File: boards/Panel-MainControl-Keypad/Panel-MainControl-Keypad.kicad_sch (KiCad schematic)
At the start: 22 parts, among them J1 Conn_01x10, J2 Conn_01x10, SW1 SW_Push, SW10 SW_Push, SW11 RotaryEncoder_Switch, SW12 RotaryEncoder_Switch, SW2 SW_Push, SW3 SW_Push, SW4 SW_Push, SW5 SW_Push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

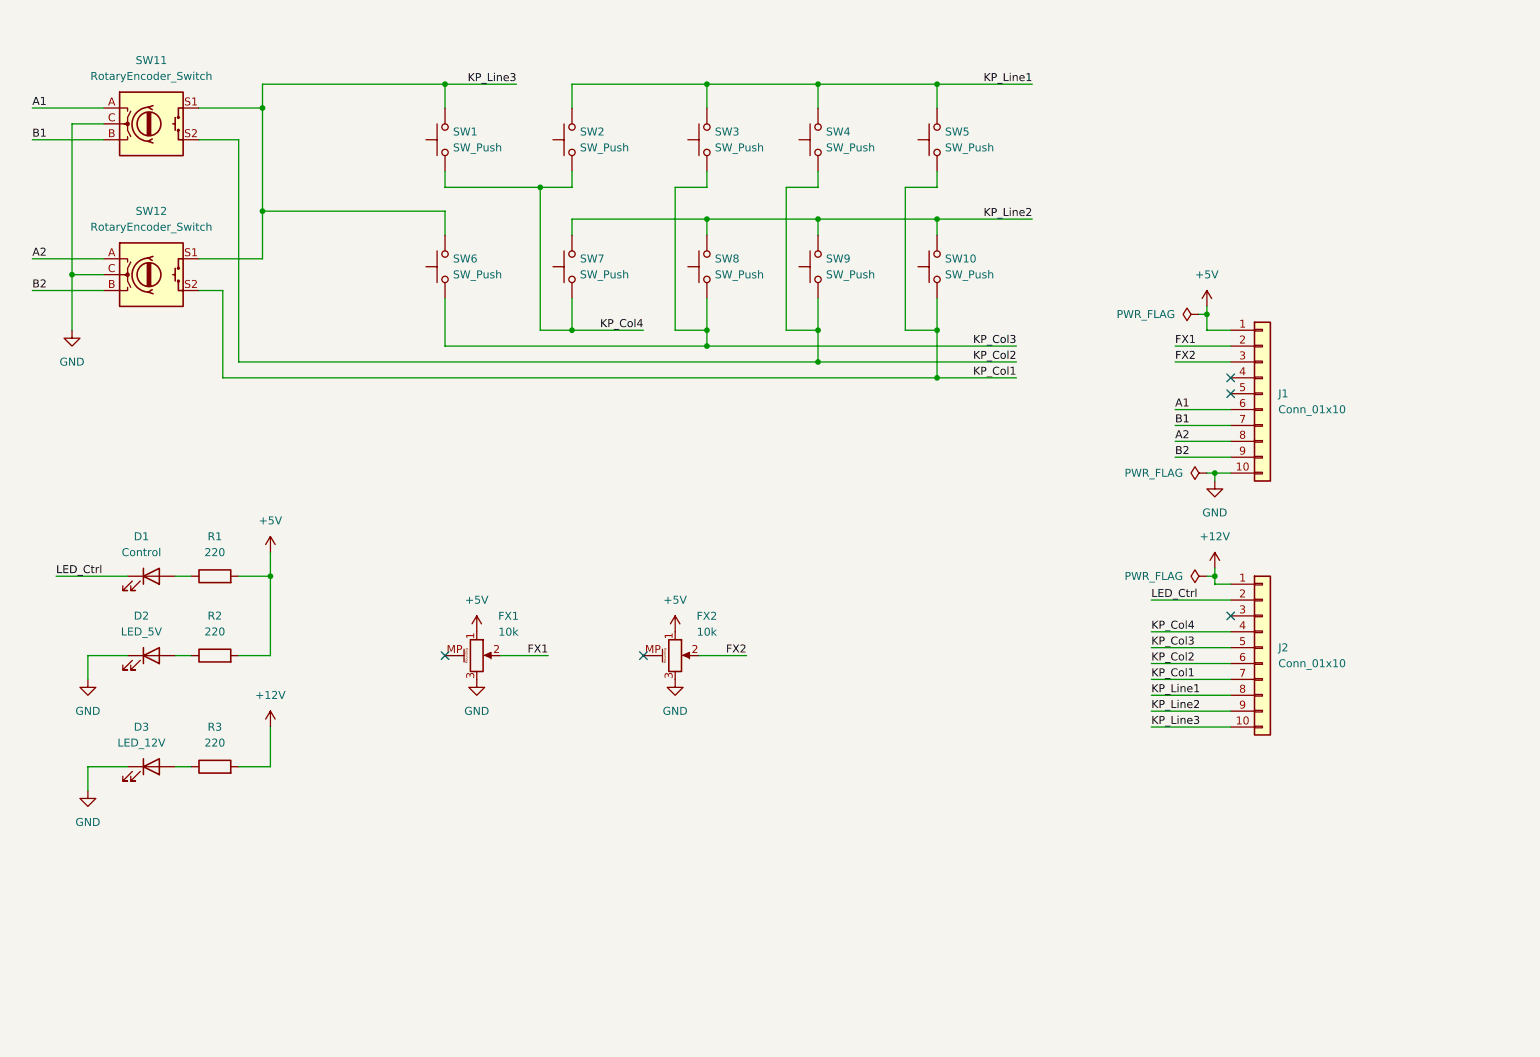
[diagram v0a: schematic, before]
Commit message: Finished PCB layouts for panel keypad
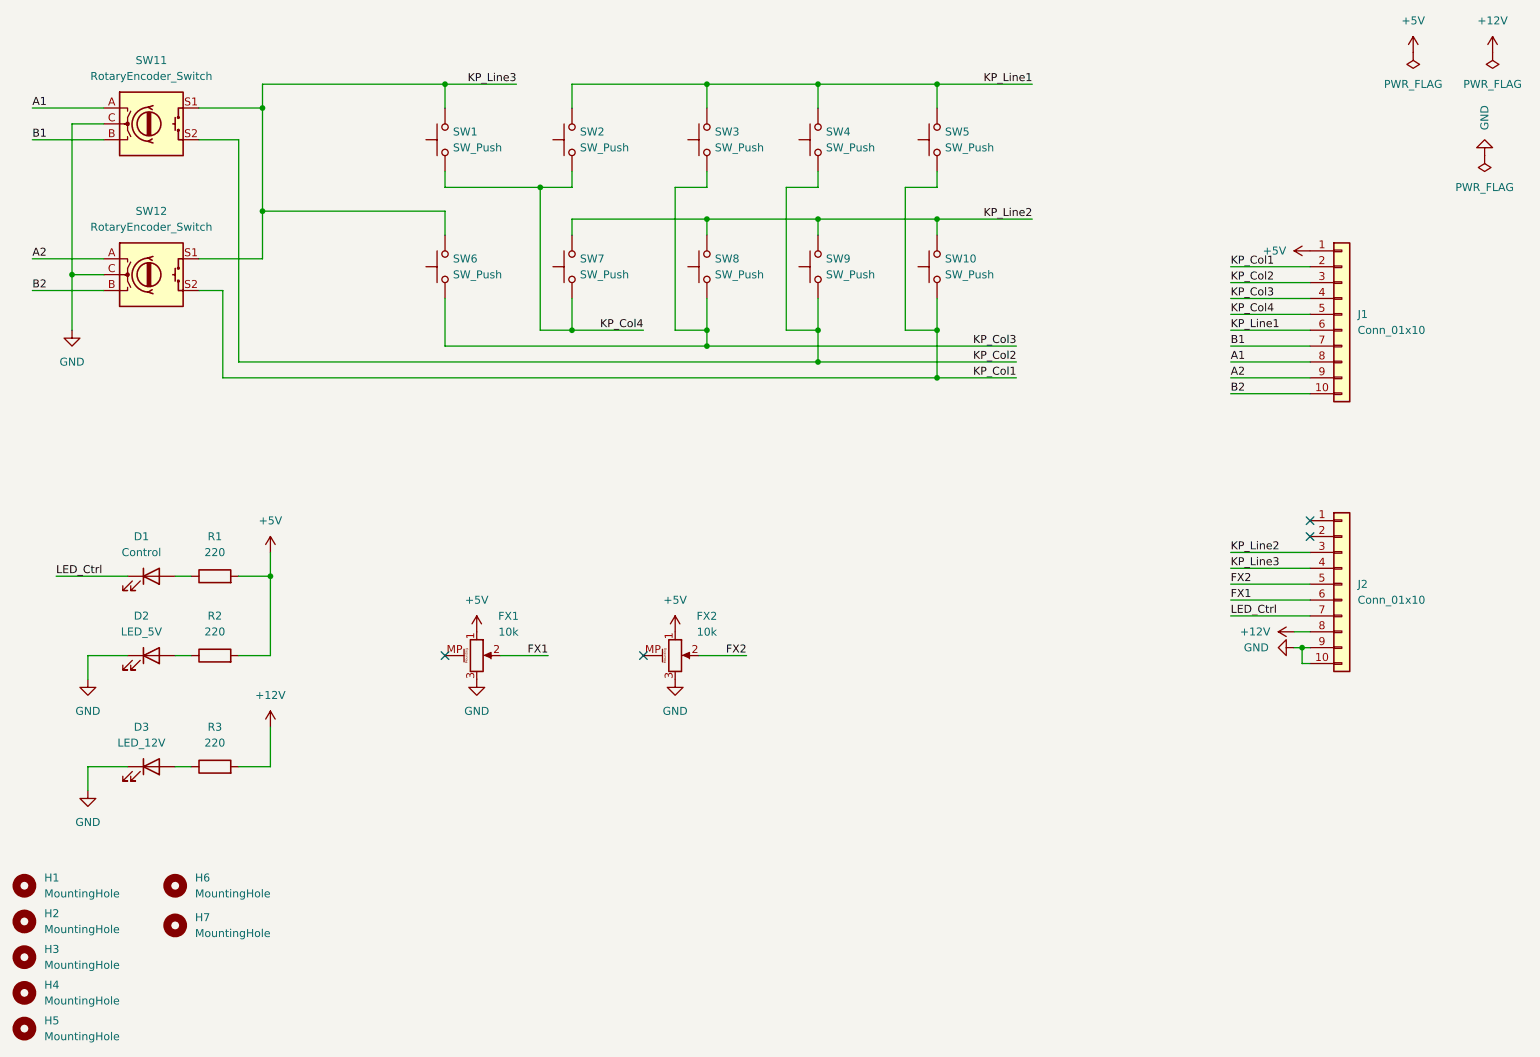
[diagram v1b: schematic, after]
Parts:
- added H1, H2, H3, H4, H5, H6, H7: MountingHole, MountingHole:MountingHole_2.7mm_M2.5, symbol Mechanical:MountingHole
- D1, D2, D3: footprint (none) -> LED_THT:LED_Rectangular_W5.0mm_H2.0mm
- J1, J2: footprint (none) -> Connector_PinHeader_2.00mm:PinHeader_1x10_P2.00mm_Vertical
- SW1, SW10, SW2, SW3, SW4, SW5, SW6, SW7, SW8, SW9: footprint Button_Switch_SMD:SW_MEC_5GSH9 -> Button_Switch_THT:SW_PUSH_6mm_H9.5mm
- SW11, SW12: footprint (none) -> SnapEDA:RotaryEncoder_Switch-PEC11R-4215F
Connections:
- net +12V: now also J2.8 (Pin_8); no longer J2.1 (Pin_1)
- net A1: now also J1.8 (Pin_8); no longer J1.6 (Pin_6)
- net A2: now also J1.9 (Pin_9); no longer J1.8 (Pin_8)
- net B2: now also J1.10 (Pin_10); no longer J1.9 (Pin_9)
- net FX1: now also J2.6 (Pin_6); no longer J1.2 (Pin_2)
- net FX2: now also J2.5 (Pin_5); no longer J1.3 (Pin_3)
- net GND: now also J2.10 (Pin_10), J2.9 (Pin_9); no longer J1.10 (Pin_10)
- net KP_Col1: now also J1.2 (Pin_2); no longer J2.7 (Pin_7)
- net KP_Col2: now also J1.3 (Pin_3); no longer J2.6 (Pin_6)
- net KP_Col3: now also J1.4 (Pin_4); no longer J2.5 (Pin_5)
- net KP_Col4: now also J1.5 (Pin_5); no longer J2.4 (Pin_4)
- net KP_Line1: now also J1.6 (Pin_6); no longer J2.8 (Pin_8)
- net KP_Line2: now also J2.3 (Pin_3); no longer J2.9 (Pin_9)
- net KP_Line3: now also J2.4 (Pin_4); no longer J2.10 (Pin_10)
- net LED_Ctrl: now also J2.7 (Pin_7); no longer J2.2 (Pin_2)
- no-connect marks 5 -> 4

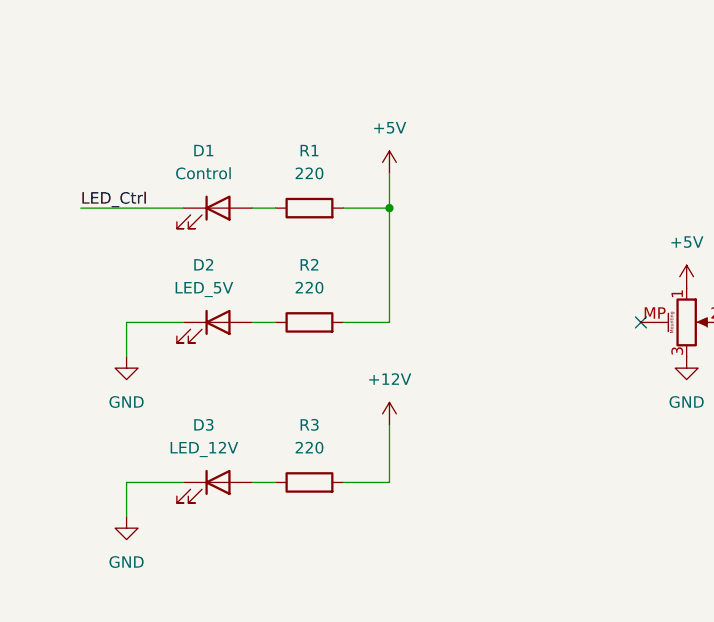
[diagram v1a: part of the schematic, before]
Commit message: Updated LED resistor values
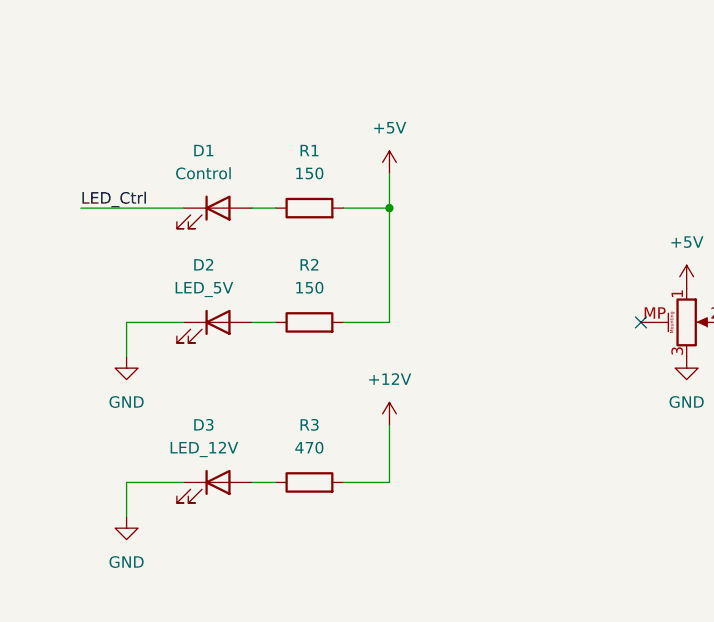
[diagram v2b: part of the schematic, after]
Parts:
- R1, R2: value 220 -> 150
- R3: value 220 -> 470
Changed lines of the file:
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@@
 			)
 		)
-		(property "Value" "220"
+		(property "Value" "150"
 			(at 59.69 110.49 90)
 			(effects
@@
 			)
 		)
-		(property "Value" "220"
+		(property "Value" "470"
 			(at 59.69 140.97 90)
 			(effects
@@
 			)
 		)
-		(property "Value" "220"
+		(property "Value" "150"
 			(at 59.69 123.19 90)
 			(effects

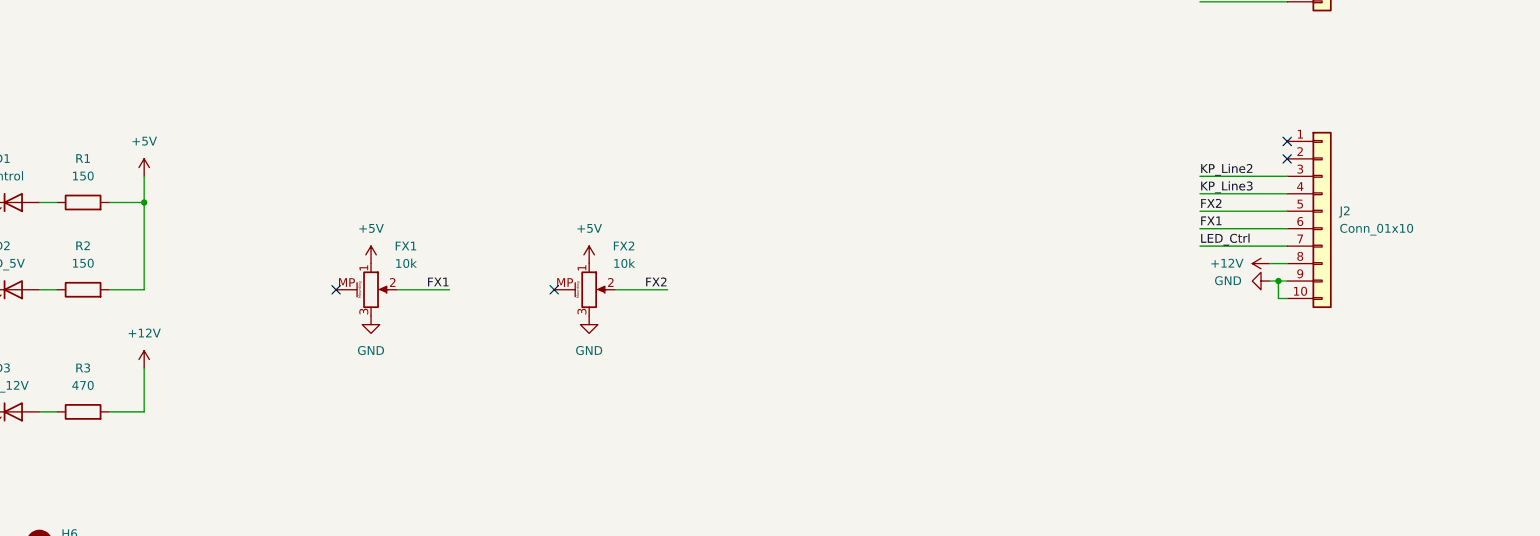
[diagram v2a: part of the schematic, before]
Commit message: Fixed using 5V from main power for PWR LED
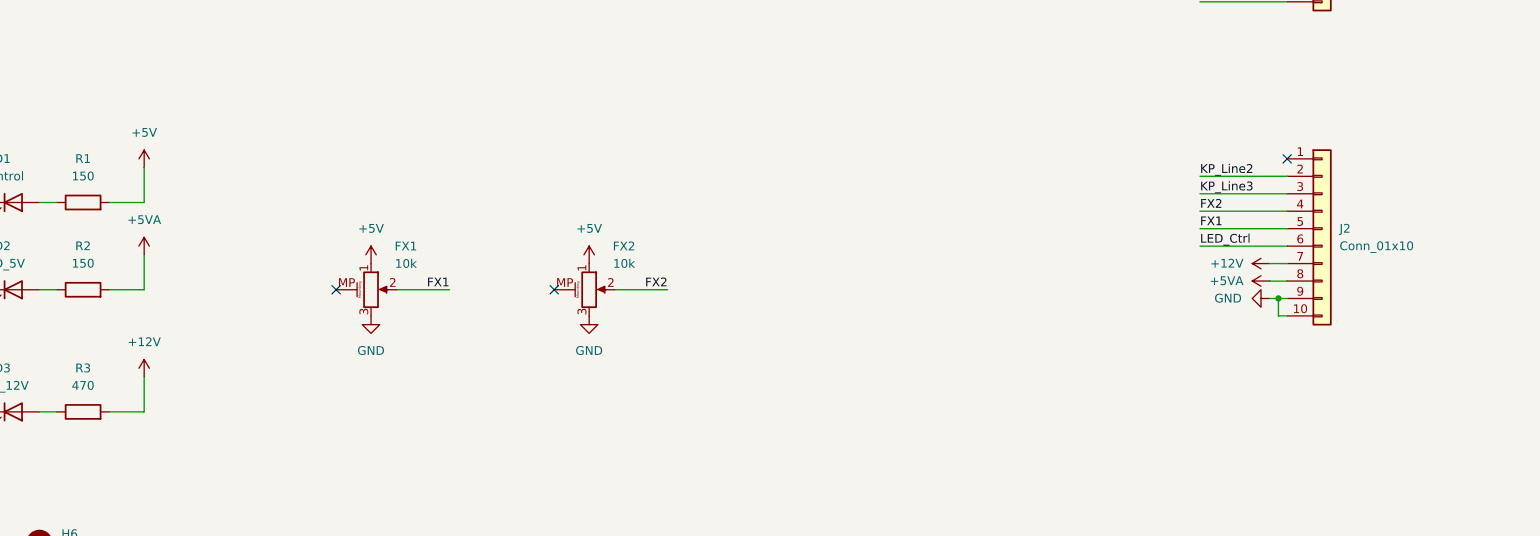
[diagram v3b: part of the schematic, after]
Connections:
- net +12V: now also J2.7 (Pin_7); no longer J2.8 (Pin_8)
- net +5V: no longer R2.2
- net FX1: now also J2.5 (Pin_5); no longer J2.6 (Pin_6)
- net FX2: now also J2.4 (Pin_4); no longer J2.5 (Pin_5)
- net KP_Line2: now also J2.2 (Pin_2); no longer J2.3 (Pin_3)
- net KP_Line3: now also J2.3 (Pin_3); no longer J2.4 (Pin_4)
- net LED_Ctrl: now also J2.6 (Pin_6); no longer J2.7 (Pin_7)
- new net +5VA: J2.8 (Pin_8), R2.2
- no-connect marks 4 -> 3
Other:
- moved on the sheet: J2
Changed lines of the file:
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@@
 	)
 	(junction
-		(at 233.68 125.73)
+		(at 233.68 128.27)
 		(diameter 0)
 		(color 0 0 0 0)
@@
 	)
 	(junction
-		(at 68.58 114.3)
-		(diameter 0)
-		(color 0 0 0 0)
-	)
-	(junction
 		(at 175.26 82.55)
 		(diameter 0)
@@
 	)
 	(no_connect
-		(at 234.95 105.41)
-	)
-	(no_connect
 		(at 234.95 107.95)
 	)
@@
 	(wire
 		(pts
+			(xy 232.41 125.73) (xy 234.95 125.73)
+		)
+		(stroke
+			(width 0)
+			(type default)
+		)
+	)
+	(wire
+		(pts
 			(xy 138.43 77.47) (xy 187.96 77.47)
 		)
@@
 	(wire
 		(pts
-			(xy 233.68 125.73) (xy 232.41 125.73)
+			(xy 233.68 128.27) (xy 232.41 128.27)
 		)
 		(stroke
@@
 	(wire
 		(pts
-			(xy 96.52 55.88) (xy 67.31 55.88)
+			(xy 68.58 121.92) (xy 68.58 127)
 		)
 		(stroke
@@
 	(wire
 		(pts
-			(xy 234.95 125.73) (xy 233.68 125.73)
+			(xy 96.52 55.88) (xy 67.31 55.88)
 		)
 		(stroke
@@
 	(wire
 		(pts
-			(xy 111.76 74.93) (xy 116.84 74.93)
+			(xy 234.95 128.27) (xy 233.68 128.27)
 		)
 		(stroke
@@
 	(wire
 		(pts
-			(xy 68.58 127) (xy 68.58 114.3)
+			(xy 111.76 74.93) (xy 116.84 74.93)
 		)
 		(stroke
@@
 	(wire
 		(pts
-			(xy 233.68 125.73) (xy 233.68 128.27)
+			(xy 233.68 128.27) (xy 233.68 130.81)
 		)
 		(stroke
@@
 	(wire
 		(pts
-			(xy 68.58 110.49) (xy 68.58 114.3)
+			(xy 68.58 109.22) (xy 68.58 114.3)
 		)
 		(stroke
@@
 	(wire
 		(pts
-			(xy 68.58 138.43) (xy 68.58 144.78)
+			(xy 68.58 139.7) (xy 68.58 144.78)
 		)
 		(stroke
@@
 	(wire
 		(pts
-			(xy 234.95 128.27) (xy 233.68 128.27)
+			(xy 234.95 130.81) (xy 233.68 130.81)
 		)
 		(stroke
@@
 	)
 	(symbol
+		(lib_id "power:+5VA")
+		(at 232.41 125.73 90)
+		(unit 1)
+		(exclude_from_sim no)
+		(in_bom yes)
+		(on_board yes)
+		(dnp no)
+		(fields_autoplaced yes)
+		(property "Reference" "#PWR016"
+			(at 236.22 125.73 0)
+			(effects
+				(font
+					(size 1.27 1.27)
+				)
+				(hide yes)
+			)
+		)
+		(property "Value" "+5VA"
+			(at 228.6 125.7299 90)
+			(effects
+				(font
+					(size 1.27 1.27)
+				)
+				(justify left)
+			)
+		)
+		(property "Footprint" ""
+			(at 232.41 125.73 0)
+			(effects
+				(font
+					(size 1.27 1.27)
+				)
+				(hide yes)
+			)
+		)
+		(property "Datasheet" ""
+			(at 232.41 125.73 0)
+			(effects
+				(font
+					(size 1.27 1.27)
+				)
+				(hide yes)
+			)
+		)
+		(property "Description" "Power symbol creates a global label with name \"+5VA\""
+			(at 232.41 125.73 0)
+			(effects
+				(font
+					(size 1.27 1.27)
+				)
+				(hide yes)
+			)
+		)
+		(pin "1"
+		)
+		(instances
+			(project "Panel-MainControl-Keypad"
+				(path "/54e31e9f-1fc3-468e-b81b-007e8e7ae7d4"
+					(reference "#PWR016")
+					(unit 1)
+				)
+			)
+		)
+	)
+	(symbol
 		(lib_id "Switch:SW_Push")
 		(at 175.26 64.77 90)
@@
 	(symbol
 		(lib_id "power:+5V")
-		(at 68.58 110.49 0)
+		(at 68.58 109.22 0)
 		(unit 1)
 		(exclude_from_sim no)
@@
 		(fields_autoplaced yes)
 		(property "Reference" "#PWR08"
-			(at 68.58 114.3 0)
+			(at 68.58 113.03 0)
 			(effects
 				(font
@@
 		)
 		(property "Value" "+5V"
-			(at 68.58 105.41 0)
+			(at 68.58 104.14 0)
 			(effects
 				(font
@@
 		)
 		(property "Footprint" ""
-			(at 68.58 110.49 0)
+			(at 68.58 109.22 0)
 			(effects
 				(font
@@
 		)
 		(property "Datasheet" ""
-			(at 68.58 110.49 0)
+			(at 68.58 109.22 0)
 			(effects
 				(font
@@
 		)
 		(property "Description" "Power symbol creates a global label with name \"+5V\""
-			(at 68.58 110.49 0)
+			(at 68.58 109.22 0)
 			(effects
 				(font
@@
 	)
 	(symbol
+		(lib_id "power:+5VA")
+		(at 68.58 121.92 0)
+		(unit 1)
+		(exclude_from_sim no)
+		(in_bom yes)
+		(on_board yes)
+		(dnp no)
+		(fields_autoplaced yes)
+		(property "Reference" "#PWR017"
+			(at 68.58 125.73 0)
+			(effects
+				(font
+					(size 1.27 1.27)
+				)
+				(hide yes)
+			)
+		)
+		(property "Value" "+5VA"
+			(at 68.58 116.84 0)
+			(effects
+				(font
+					(size 1.27 1.27)
+				)
+			)
+		)
+		(property "Footprint" ""
+			(at 68.58 121.92 0)
+			(effects
+				(font
+					(size 1.27 1.27)
+				)
+				(hide yes)
+			)
+		)
+		(property "Datasheet" ""
+			(at 68.58 121.92 0)
+			(effects
+				(font
+					(size 1.27 1.27)
+				)
+				(hide yes)
+			)
+		)
+		(property "Description" "Power symbol creates a global label with name \"+5VA\""
+			(at 68.58 121.92 0)
+			(effects
+				(font
+					(size 1.27 1.27)
+				)
+				(hide yes)
+			)
+		)
+		(pin "1"
+		)
+		(instances
+			(project "Panel-MainControl-Keypad"
+				(path "/54e31e9f-1fc3-468e-b81b-007e8e7ae7d4"
+					(reference "#PWR017")
+					(unit 1)
+				)
+			)
+		)
+	)
+	(symbol
 		(lib_id "power:+12V")
 		(at 232.41 123.19 90)
@@
 	(symbol
 		(lib_id "power:GND")
-		(at 232.41 125.73 270)
+		(at 232.41 128.27 270)
 		(unit 1)
 		(exclude_from_sim no)
@@
 		(dnp no)
 		(property "Reference" "#PWR010"
-			(at 226.06 125.73 0)
+			(at 226.06 128.27 0)
 			(effects
 				(font
@@
 		)
 		(property "Value" "GND"
-			(at 228.346 125.73 90)
+			(at 228.346 128.27 90)
 			(effects
 				(font
@@
 		)
 		(property "Footprint" ""
-			(at 232.41 125.73 0)
+			(at 232.41 128.27 0)
 			(effects
 				(font
@@
 		)
 		(property "Datasheet" ""
-			(at 232.41 125.73 0)
+			(at 232.41 128.27 0)
 			(effects
 				(font
@@
 		)
 		(property "Description" "Power symbol creates a global label with name \"GND\" , ground"
-			(at 232.41 125.73 0)
+			(at 232.41 128.27 0)
 			(effects
 				(font
@@
 	(symbol
 		(lib_id "power:+12V")
-		(at 68.58 138.43 0)
+		(at 68.58 139.7 0)
 		(unit 1)
 		(exclude_from_sim no)
@@
 		(fields_autoplaced yes)
 		(property "Reference" "#PWR012"
-			(at 68.58 142.24 0)
+			(at 68.58 143.51 0)
 			(effects
 				(font
@@
 		)
 		(property "Value" "+12V"
-			(at 68.58 133.35 0)
+			(at 68.58 134.62 0)
 			(effects
 				(font
@@
 		)
 		(property "Footprint" ""
-			(at 68.58 138.43 0)
+			(at 68.58 139.7 0)
 			(effects
 				(font
@@
 		)
 		(property "Datasheet" ""
-			(at 68.58 138.43 0)
+			(at 68.58 139.7 0)
 			(effects
 				(font
@@
 		)
 		(property "Description" "Power symbol creates a global label with name \"+12V\""
-			(at 68.58 138.43 0)
+			(at 68.58 139.7 0)
 			(effects
 				(font
@@
 	(symbol
 		(lib_id "Connector_Generic:Conn_01x10")
-		(at 240.03 115.57 0)
+		(at 240.03 118.11 0)
 		(unit 1)
 		(exclude_from_sim no)
@@
 		(fields_autoplaced yes)
 		(property "Reference" "J2"
-			(at 242.57 115.5699 0)
+			(at 242.57 118.1099 0)
 			(effects
 				(font
@@
 		)
 		(property "Value" "Conn_01x10"
-			(at 242.57 118.1099 0)
+			(at 242.57 120.6499 0)
 			(effects
 				(font
@@
 		)
 		(property "Footprint" "Connector_PinHeader_2.00mm:PinHeader_1x10_P2.00mm_Vertical"
-			(at 240.03 115.57 0)
+			(at 240.03 118.11 0)
 			(effects
 				(font
@@
 		)
 		(property "Datasheet" "~"
-			(at 240.03 115.57 0)
+			(at 240.03 118.11 0)
 			(effects
 				(font
@@
 		)
 		(property "Description" "Generic connector, single row, 01x10, script generated (kicad-library-utils/schlib/autogen/connector/)"
-			(at 240.03 115.57 0)
+			(at 240.03 118.11 0)
 			(effects
 				(font
